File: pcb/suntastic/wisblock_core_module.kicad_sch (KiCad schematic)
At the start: 23 parts, among them J4 FBB04004-F40S1003K6M, J7 Conn_01x04_Pin, J8 Conn_01x04_Pin, J9 Conn_01x08_Pin

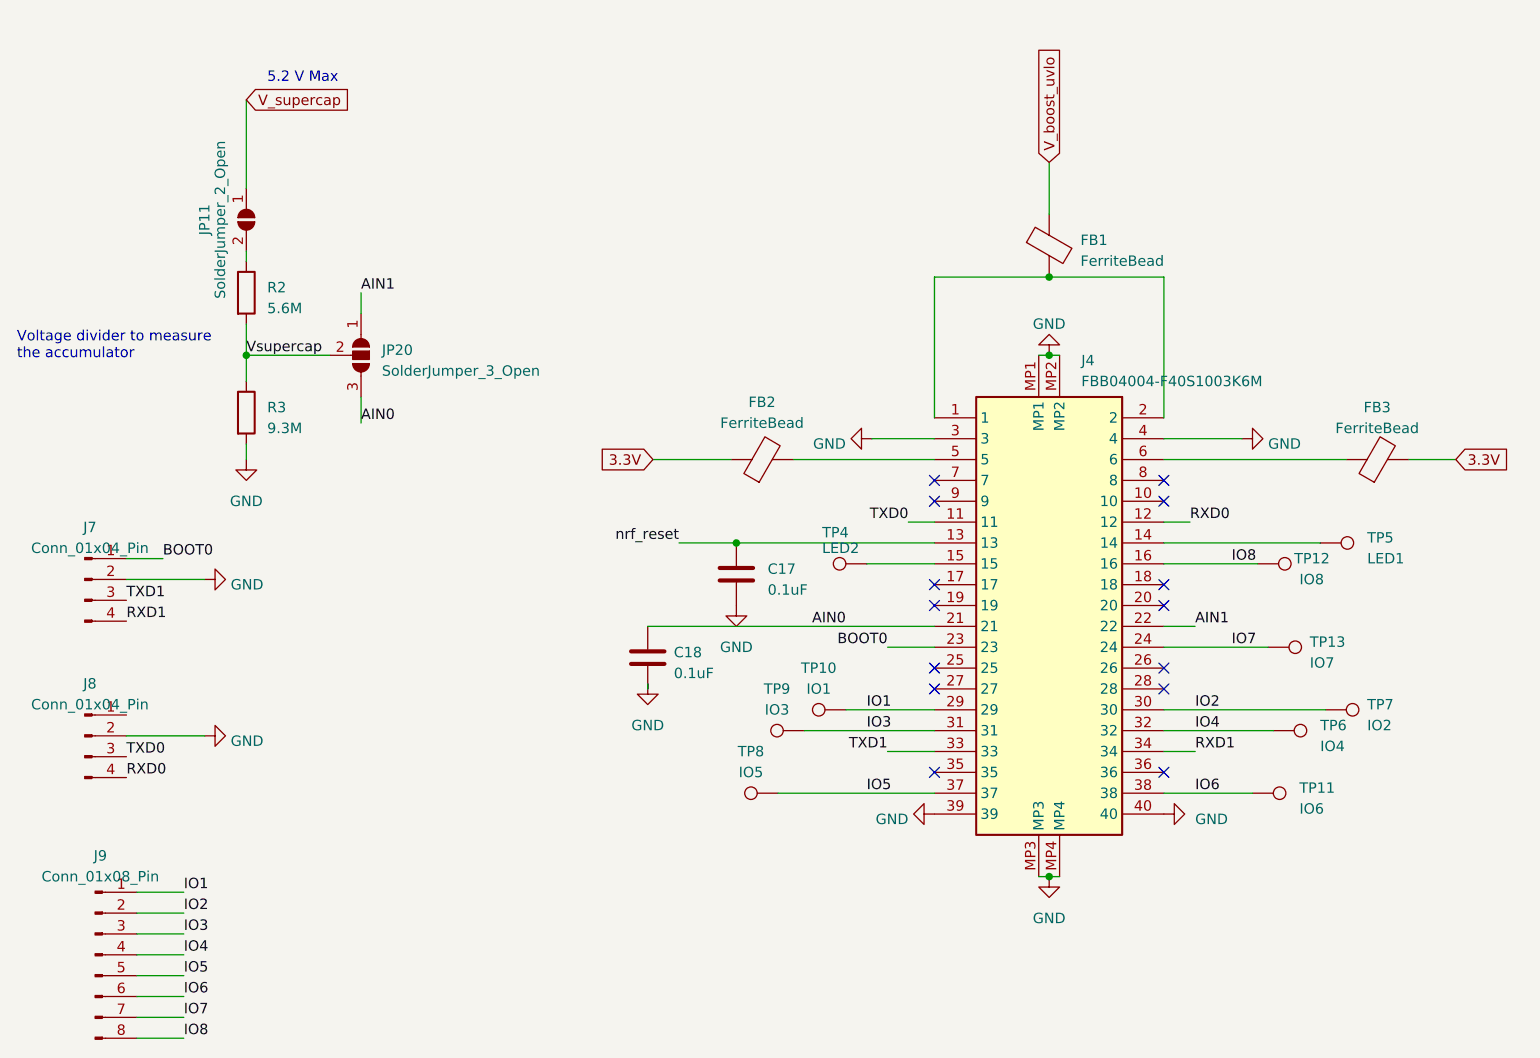
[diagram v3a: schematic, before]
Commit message: Update footprints
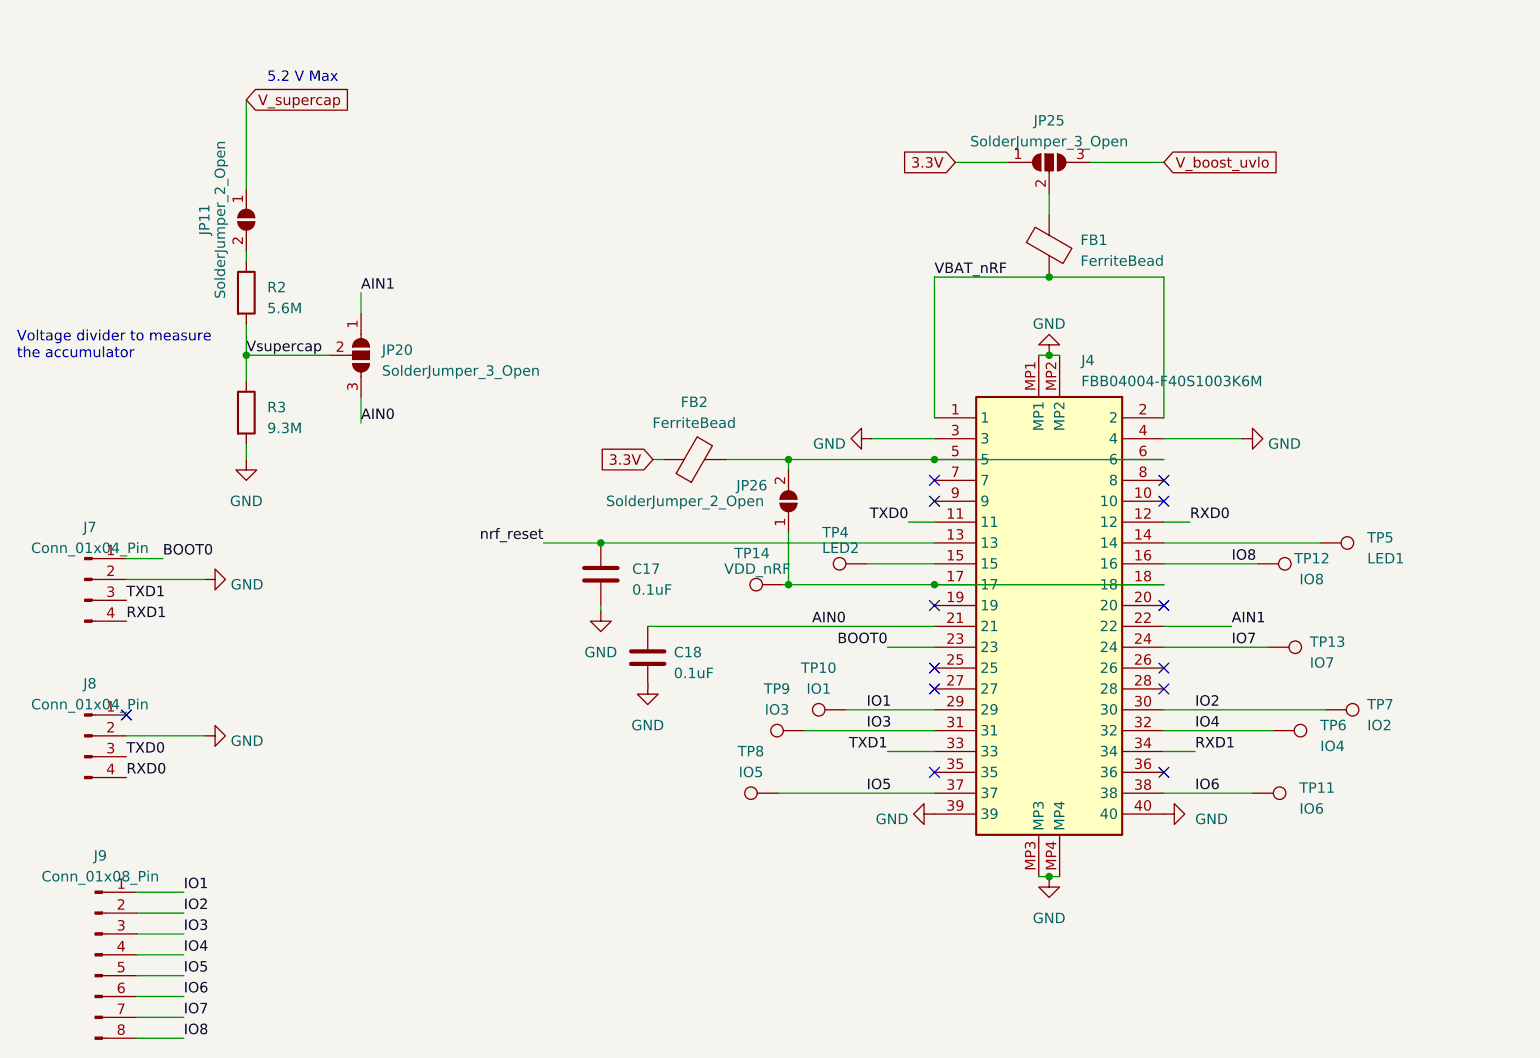
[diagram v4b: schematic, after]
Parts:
- removed FB3: FerriteBead, symbol Device:FerriteBead
- added JP25: SolderJumper_3_Open, Jumper:SolderJumper-3_P1.3mm_Open_RoundedPad1.0x1.5mm_NumberLabels, symbol Jumper:SolderJumper_3_Open
- added JP26: SolderJumper_2_Open, Jumper:SolderJumper-2_P1.3mm_Open_RoundedPad1.0x1.5mm, symbol Jumper:SolderJumper_2_Open
- added TP14: VDD_nRF, TestPoint:TestPoint_Pad_D1.5mm, symbol Connector:TestPoint
- C17, C18: footprint (none) -> Capacitor_SMD:C_0603_1608Metric_Pad1.08x0.95mm_HandSolder
- J7, J8: footprint (none) -> Connector_PinHeader_2.54mm:PinHeader_1x04_P2.54mm_Vertical
- J9: footprint (none) -> Connector_PinHeader_2.54mm:PinHeader_1x08_P2.54mm_Vertical
- JP20: footprint (none) -> Jumper:SolderJumper-3_P1.3mm_Open_RoundedPad1.0x1.5mm_NumberLabels
- R2, R3: footprint (none) -> Resistor_SMD:R_0603_1608Metric_Pad0.98x0.95mm_HandSolder
- TP10, TP11, TP12, TP13, TP4, TP5, TP6, TP7, TP8, TP9: footprint (none) -> TestPoint:TestPoint_Pad_D1.5mm
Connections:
- net 3.3V: now also JP25.1 (A)
- net V_boost_uvlo: now also JP25.3 (B); no longer FB1.1
- net at J4.6: now also FB2.2, J4.5, JP26.2 (B)
- net VBAT_nRF: now reaches FB1.2, J4.1, J4.2
- net at J4.17: now also J4.18, JP26.1 (A), TP14.1
- new net: FB1.1, JP25.2 (C)
- no-connect marks 14 -> 13
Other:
- moved on the sheet: C17, FB2

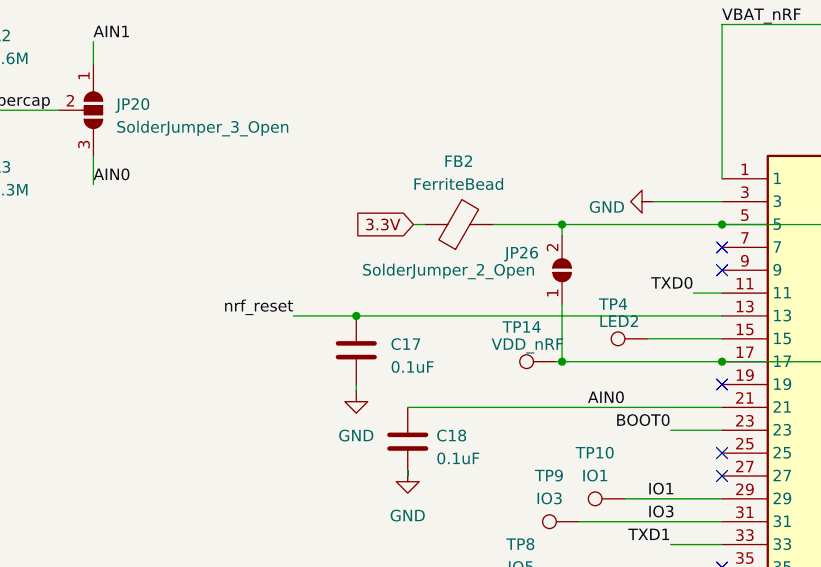
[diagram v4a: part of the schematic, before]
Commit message: Update more footprints and start with PCB
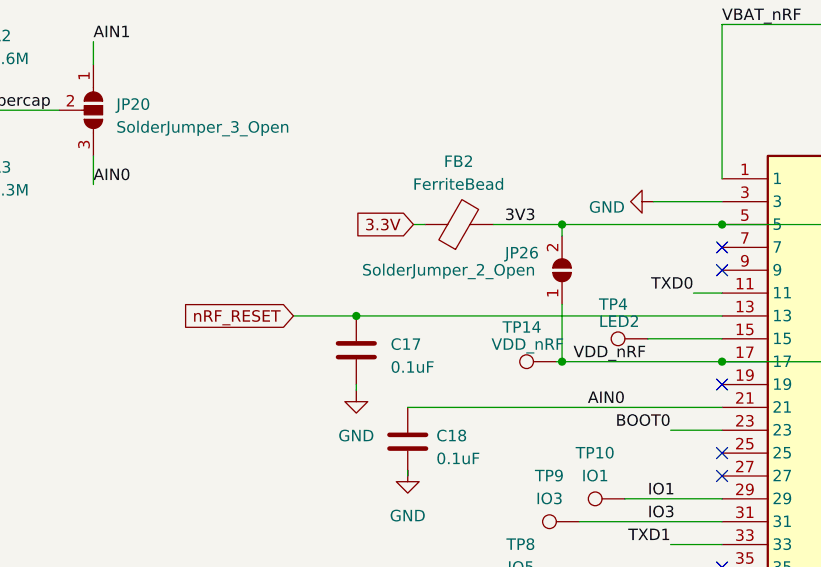
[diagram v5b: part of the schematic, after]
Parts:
- FB1, FB2: footprint (none) -> Inductor_SMD:L_0603_1608Metric_Pad1.05x0.95mm_HandSolder
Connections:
- net VDD_nRF: now reaches J4.17, J4.18, JP26.1 (A), TP14.1
- net 3V3: now reaches FB2.2, J4.5, J4.6, JP26.2 (B)
- net nrf_reset renamed nRF_RESET
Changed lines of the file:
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@@
     (effects (font (size 1.27 1.27)) (justify right bottom))
+  )
+  (label "VDD_nRF" (at 109.22 78.74 0) (fields_autoplaced)
+    (effects (font (size 1.27 1.27)) (justify left bottom))
   )
   (label "IO6" (at 157.48 104.14 0) (fields_autoplaced)
@@
     (effects (font (size 1.27 1.27)) (justify left bottom))
   )
-  (label "nrf_reset" (at 78.105 73.66 180) (fields_autoplaced)
-    (effects (font (size 1.27 1.27)) (justify right bottom))
-  )
   (label "IO1" (at 117.475 93.98 0) (fields_autoplaced)
     (effects (font (size 1.27 1.27)) (justify left bottom))
@@
   )
   (label "TXD0" (at 27.305 99.695 0) (fields_autoplaced)
+    (effects (font (size 1.27 1.27)) (justify left bottom))
+  )
+  (label "3V3" (at 101.6 63.5 0) (fields_autoplaced)
     (effects (font (size 1.27 1.27)) (justify left bottom))
   )
@@
     )
   )
+  (global_label "nRF_RESET" (shape input) (at 78.105 73.66 180) (fields_autoplaced)
+    (effects (font (size 1.27 1.27)) (justify right))
+    (property "Intersheetrefs" "${INTERSHEET_REFS}" (at 64.9789 73.66 0)
+      (effects (font (size 1.27 1.27)) (justify right) hide)
+    )
+  )
   (symbol (lib_id "power:GND") (at 41.91 63.5 0) (unit 1)
     (in_bom yes) (on_board yes) (dnp no) (fields_autoplaced)
@@
       (effects (font (size 1.27 1.27)))
     )
-    (property "Footprint" "" (at 96.52 65.278 90)
+    (property "Footprint" "Inductor_SMD:L_0603_1608Metric_Pad1.05x0.95mm_HandSolder" (at 96.52 65.278 90)
       (effects (font (size 1.27 1.27)) hide)
     )
@@
       (effects (font (size 1.27 1.27)) (justify left))
     )
-    (property "Footprint" "" (at 137.922 37.465 90)
-      (effects (font (size 1.27 1.27)) hide)
-    )
+    (property "Footprint" "Inductor_SMD:L_0603_1608Metric_Pad1.05x0.95mm_HandSolder" (at 137.922 37.465 90)
+      (effects (font (size 1.27 1.27)) hide)
+    )

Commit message: Rework watchdog
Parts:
- removed TP10: IO1, TestPoint:TestPoint_Pad_D1.5mm, symbol Connector:TestPoint
- removed TP11: IO6, TestPoint:TestPoint_Pad_D1.5mm, symbol Connector:TestPoint
- removed TP12: IO8, TestPoint:TestPoint_Pad_D1.5mm, symbol Connector:TestPoint
- removed TP13: IO7, TestPoint:TestPoint_Pad_D1.5mm, symbol Connector:TestPoint
- removed TP14: VDD_nRF, TestPoint:TestPoint_Pad_D1.5mm, symbol Connector:TestPoint
- removed TP6: IO4, TestPoint:TestPoint_Pad_D1.5mm, symbol Connector:TestPoint
- removed TP7: IO2, TestPoint:TestPoint_Pad_D1.5mm, symbol Connector:TestPoint
- removed TP8: IO5, TestPoint:TestPoint_Pad_D1.5mm, symbol Connector:TestPoint
- removed TP9: IO3, TestPoint:TestPoint_Pad_D1.5mm, symbol Connector:TestPoint
- TP5: footprint TestPoint:TestPoint_Pad_D1.5mm -> TestPoint:TestPoint_Pad_D1.0mm
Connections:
- net IO2: now also J9.6 (Pin_6); no longer J9.2 (Pin_2)
- net IO4: now also J9.5 (Pin_5); no longer J9.4 (Pin_4)
- net IO5: now also J9.2 (Pin_2); no longer J9.5 (Pin_5)
- net IO6: now also J9.4 (Pin_4); no longer J9.6 (Pin_6)
